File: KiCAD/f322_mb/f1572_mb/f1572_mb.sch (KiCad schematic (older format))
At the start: 24 parts, among them Q1 2N3904, SW1 power, SW2 ~rst, U1 PIC12F1572, U2 LM386

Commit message: debugging and adding melodies
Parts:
- removed C5: 1µF, symbol device:CP
- removed C6: 47n, symbol device:C
- removed C7: 220µF, symbol device:CP
- removed R4, R5, R6: 100R, symbol device:R
- removed RV1: 10K, symbol device:POT
- removed U2: LM386, symbol linear:LM386
- removed X?: 8Mhz, Oscillators:Oscillator_DIP-8, symbol Oscillators:CXO_DIP8
- added C1: 100µF, symbol device:CP
- added D1: 1N4001, symbol device:D
- added D2: RED, symbol device:LED
- added D3, D4: 1N4148, symbol device:D
- added D5, D6: GRN/RED, symbol device:LED_Dual_AAC
- added R2: 470R, symbol device:R
- added R3: 3K3, symbol device:R
- added R9: 220R, symbol device:R
- BT1: value 4,5v -> 6v
- C5: renamed from C4; value 220µF -> 100µF
- R8: value 10R -> 220R
- renumbered C1 to C2, C2 to C3, C3 to C4, R2 to R4, R3 to R5
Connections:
- net GND: now also R8.2, C1.2, R9.2; no longer R8.1
- net Vdd: now also D1.1 (K), R2.2; no longer SW1.2 (B)
- net at R4.2: now also U1.6 (RA1), R3.2; no longer U1.3 (RA4)
- net at U1.5 (RA2): now also D2.1 (K)
- net at U1.7 (RA0): now also Q1.2 (C)
- net at C4.1, R5.2: now also D3.2 (A), D4.1 (K); no longer R4.1
- net at LS1.1: now also C5.2
- net CLKIN renamed RA5
- net RA5: now also D5.1 (A1), D6.2 (A2)
- new net: D4.2 (A), R4.1
- new net: D2.2 (A), R2.1
- new net: D3.1 (K), R3.1
- new net: D5.3 (K), R8.1
- new net: D6.3 (K), R9.1
- new net RA4: D5.2 (A2), D6.1 (A1), U1.3 (RA4)
- new net Vbatt: C1.1, D1.2 (A), SW1.2 (B)
- no-connect marks 1 -> 0
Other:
- moved on the sheet: BT1, C4, LS1, R4, R5, SW1, SW2

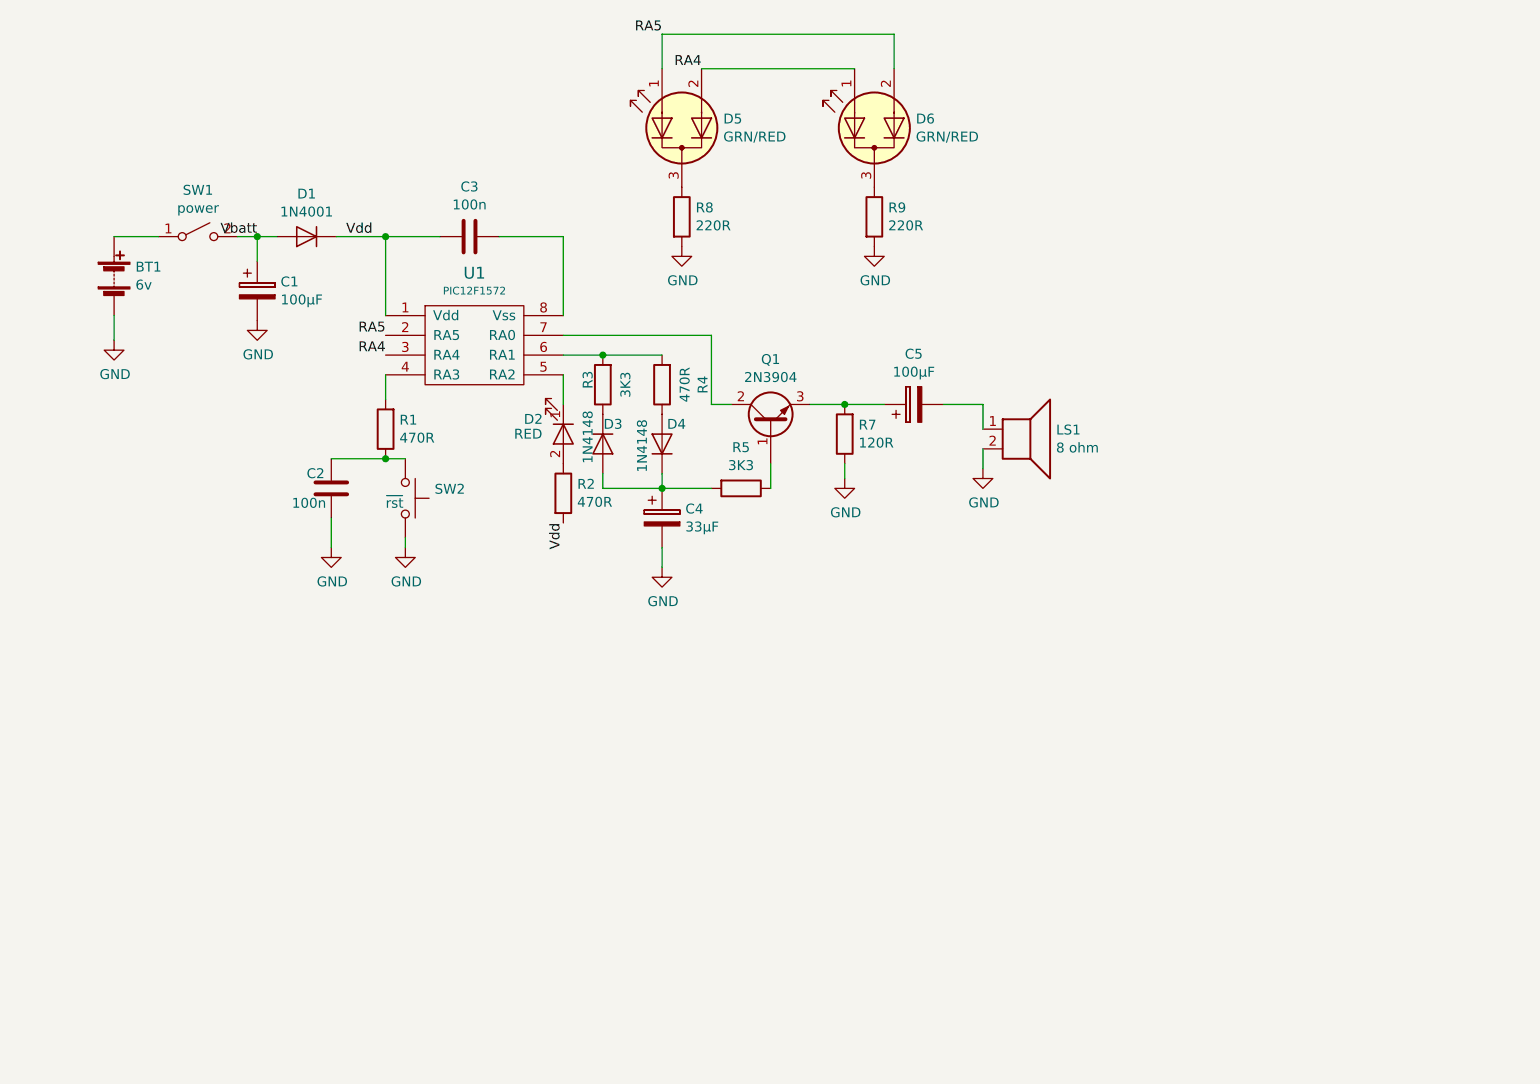
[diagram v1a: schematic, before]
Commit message: modification to cicircuit diagram. Switched PWM between LED and ENV
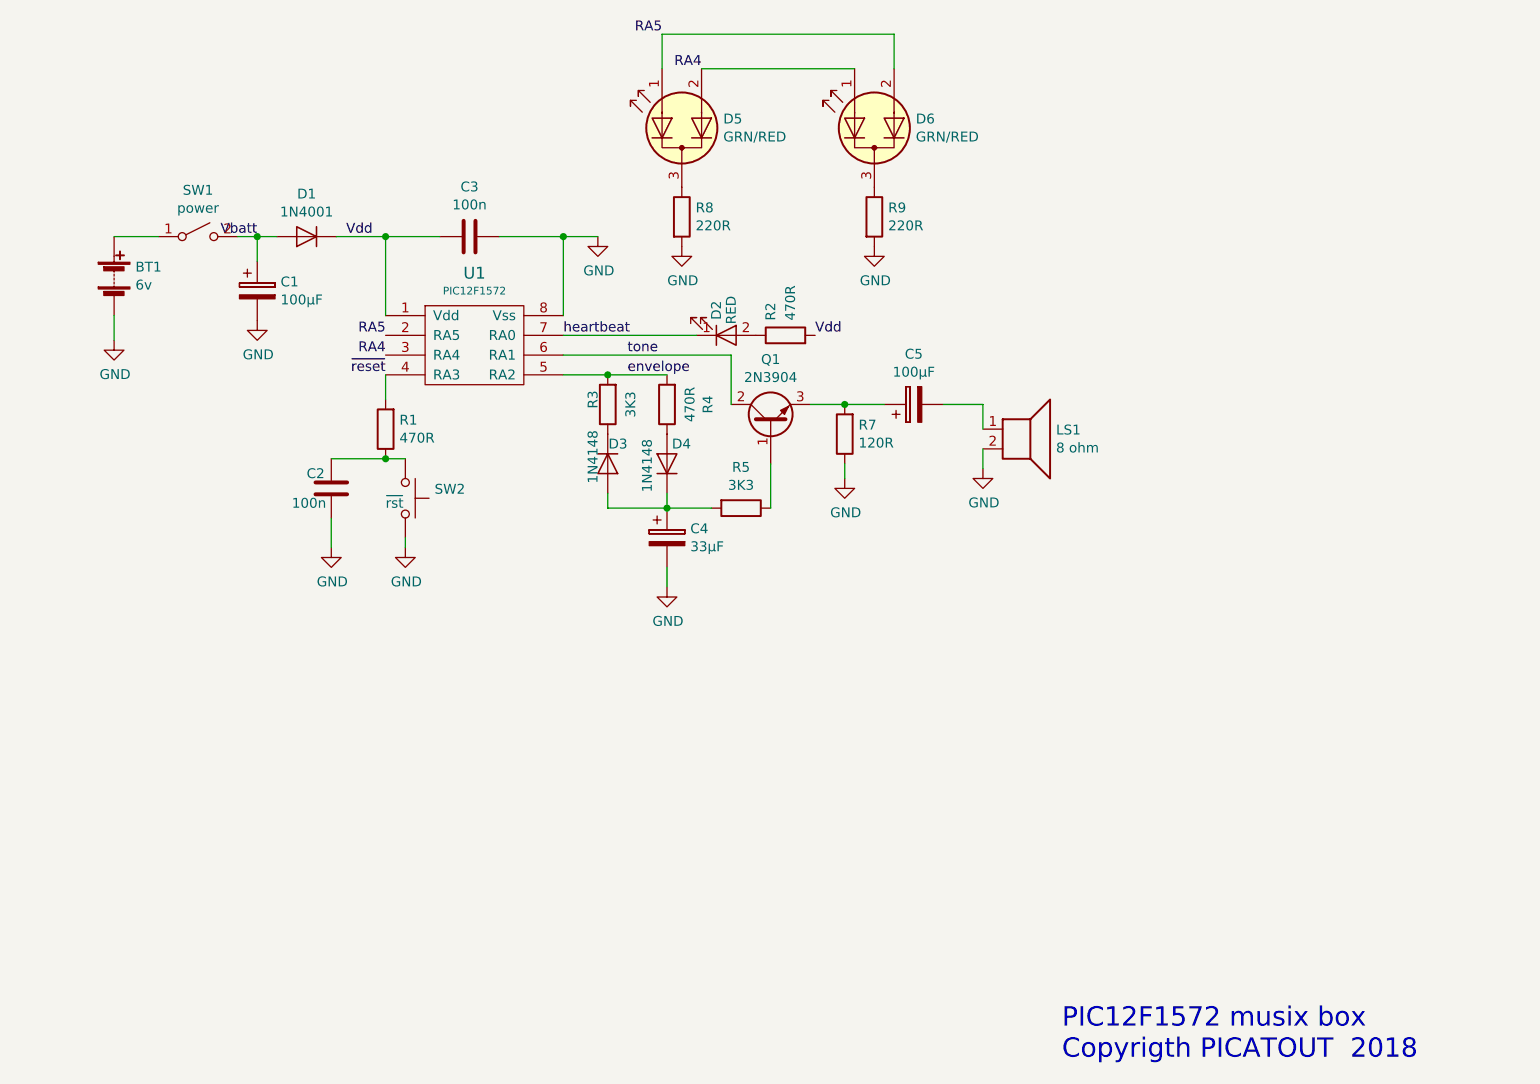
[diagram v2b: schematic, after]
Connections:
- net GND: now also C3.1, U1.8 (Vss)
- net ~reset: now reaches R1.2, U1.4 (RA3)
- net envelope: now reaches U1.5 (RA2)
- net envelope: now also R3.2, R4.2; no longer D2.1 (K)
- net heartbeat: now reaches U1.7 (RA0)
- net heartbeat: now also D2.1 (K); no longer Q1.2 (C)
- new net tone: Q1.2 (C), U1.6 (RA1)
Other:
- note added: "PIC12F1572 musix box\nCopyrigth PICATOUT 2018"
- moved on the sheet: C4, D2, D3, D4, R2, R3, R4, R5
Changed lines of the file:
@@
 	0    -1   -1   0
 $EndComp
-Wire Wire Line
-	5500 3275 5500 3625
-Wire Wire Line
-	5500 3625 5600 3625
 $Comp
 L device:R R7
@@
 L device:R R5
 U 1 1 5C07471B
-P 5650 4050
-F 0 "R5" V 5443 4050 50  0000 C CNN
-F 1 "3K3" V 5534 4050 50  0000 C CNN
-F 2 "" V 5580 4050 50  0001 C CNN
-F 3 "" H 5650 4050 50  0001 C CNN
-	1    5650 4050
+P 5650 4150
+F 0 "R5" V 5443 4150 50  0000 C CNN
+F 1 "3K3" V 5534 4150 50  0000 C CNN
+F 2 "" V 5580 4150 50  0001 C CNN
+F 3 "" H 5650 4150 50  0001 C CNN
+	1    5650 4150
 	0    1    1    0
 $EndComp
@@
 L device:CP C4
 U 1 1 5C07494D
-P 5250 4200
-F 0 "C4" H 5368 4246 50  0000 L CNN
-F 1 "33µF" H 5368 4155 50  0000 L CNN
-F 2 "" H 5288 4050 50  0001 C CNN
-F 3 "" H 5250 4200 50  0001 C CNN
-	1    5250 4200
+P 5275 4300
+F 0 "C4" H 5393 4346 50  0000 L CNN
+F 1 "33µF" H 5393 4255 50  0000 L CNN
+F 2 "" H 5313 4150 50  0001 C CNN
+F 3 "" H 5275 4300 50  0001 C CNN
+	1    5275 4300
 	1    0    0    -1
 $EndComp
@@
 L power:GND #PWR05
 U 1 1 5C0749C3
-P 5250 4450
-F 0 "#PWR05" H 5250 4200 50  0001 C CNN
-F 1 "GND" H 5255 4277 50  0000 C CNN
-F 2 "" H 5250 4450 50  0001 C CNN
-F 3 "" H 5250 4450 50  0001 C CNN
-	1    5250 4450
-	1    0    0    -1
-$EndComp
-Wire Wire Line
-	5250 4350 5250 4450
-Wire Wire Line
-	5250 4050 5500 4050
+P 5275 4550
+F 0 "#PWR05" H 5275 4300 50  0001 C CNN
+F 1 "GND" H 5280 4377 50  0000 C CNN
+F 2 "" H 5275 4550 50  0001 C CNN
+F 3 "" H 5275 4550 50  0001 C CNN
+	1    5275 4550
+	1    0    0    -1
+$EndComp
+Wire Wire Line
+	5275 4450 5275 4550
 $Comp
 L device:R R4
 U 1 1 5C074DC4
-P 5250 3525
-F 0 "R4" V 5043 3525 50  0000 C CNN
-F 1 "470R" V 5134 3525 50  0000 C CNN
-F 2 "" V 5180 3525 50  0001 C CNN
-F 3 "" H 5250 3525 50  0001 C CNN
-	1    5250 3525
+P 5275 3625
+F 0 "R4" V 5068 3625 50  0000 C CNN
+F 1 "470R" V 5159 3625 50  0000 C CNN
+F 2 "" V 5205 3625 50  0001 C CNN
+F 3 "" H 5275 3625 50  0001 C CNN
+	1    5275 3625
 	-1   0    0    1
 $EndComp
@@
 	6175 3625 6375 3625
 Connection ~ 6175 3625
-Wire Wire Line
-	4750 3275 5500 3275
-Wire Wire Line
-	5800 3925 5800 4050
-Connection ~ 5250 4050
-$Comp
-L device:LED D2
-U 1 1 5C099DC3
-P 4750 3775
-F 0 "D2" V 4675 3575 50  0000 L CNN
-F 1 "RED" V 4750 3525 50  0000 L CNN
-F 2 "" H 4750 3775 50  0001 C CNN
-F 3 "" H 4750 3775 50  0001 C CNN
-	1    4750 3775
-	0    1    1    0
-$EndComp
-Wire Wire Line
-	4750 3475 4750 3625
+Connection ~ 5275 4150
 $Comp
 L device:R R2
 U 1 1 5C09AC95
-P 4750 4075
-F 0 "R2" H 4820 4121 50  0000 L CNN
-F 1 "470R" H 4820 4030 50  0000 L CNN
-F 2 "" V 4680 4075 50  0001 C CNN
-F 3 "" H 4750 4075 50  0001 C CNN
-	1    4750 4075
-	1    0    0    -1
-$EndComp
-Text Label 4750 4225 3    50   ~ 0
+P 5875 3275
+F 0 "R2" H 5950 3350 50  0000 L CNN
+F 1 "470R" H 5950 3250 50  0000 L CNN
+F 2 "" V 5805 3275 50  0001 C CNN
+F 3 "" H 5875 3275 50  0001 C CNN
+	1    5875 3275
+	0    -1   -1   0
+$EndComp
+Text Label 6025 3275 0    50   ~ 0
 Vdd
 $Comp
 L device:D D4
 U 1 1 5C09B843
-P 5250 3825
-F 0 "D4" V 5350 3800 50  0000 R CNN
-F 1 "1N4148" H 5375 3925 50  0000 R CNN
-F 2 "" H 5250 3825 50  0001 C CNN
-F 3 "" H 5250 3825 50  0001 C CNN
-	1    5250 3825
-	0    -1   -1   0
-$EndComp
-Wire Wire Line
-	4750 3375 4950 3375
-Wire Wire Line
-	5250 3975 5250 4050
+P 5275 3925
+F 0 "D4" V 5375 3900 50  0000 R CNN
+F 1 "1N4148" H 5400 4025 50  0000 R CNN
+F 2 "" H 5275 3925 50  0001 C CNN
+F 3 "" H 5275 3925 50  0001 C CNN
+	1    5275 3925
+	0    -1   -1   0
+$EndComp
+Wire Wire Line
+	5275 4075 5275 4150
 $Comp
 L device:R R3
 U 1 1 5C0B54FF
-P 4950 3525
-F 0 "R3" V 5025 3500 50  0000 C CNN
-F 1 "3K3" V 4834 3525 50  0000 C CNN
-F 2 "" V 4880 3525 50  0001 C CNN
-F 3 "" H 4950 3525 50  0001 C CNN
-	1    4950 3525
-	-1   0    0    1
-$EndComp
-Connection ~ 4950 3375
-Wire Wire Line
-	4950 3375 5250 3375
+P 4975 3625
+F 0 "R3" V 5050 3600 50  0000 C CNN
+F 1 "3K3" V 4859 3625 50  0000 C CNN
+F 2 "" V 4905 3625 50  0001 C CNN
+F 3 "" H 4975 3625 50  0001 C CNN
+	1    4975 3625
+	-1   0    0    1
+$EndComp
+Wire Wire Line
+	4975 3475 5275 3475
 $Comp
 L device:D D3
 U 1 1 5C0B56CF
-P 4950 3825
-F 0 "D3" V 4850 3925 50  0000 R CNN
-F 1 "1N4148" H 5050 3750 50  0000 R CNN
-F 2 "" H 4950 3825 50  0001 C CNN
-F 3 "" H 4950 3825 50  0001 C CNN
-	1    4950 3825
+P 4975 3925
+F 0 "D3" V 4875 4025 50  0000 R CNN
+F 1 "1N4148" H 5075 3850 50  0000 R CNN
+F 2 "" H 4975 3925 50  0001 C CNN
+F 3 "" H 4975 3925 50  0001 C CNN
+	1    4975 3925
 	0    1    1    0
 $EndComp
 Wire Wire Line
-	4950 3975 4950 4050
-Wire Wire Line
-	4950 4050 5250 4050
+	4975 4075 4975 4150
+Wire Wire Line
+	4975 4150 5275 4150
 Text Label 5250 1750 2    50   ~ 0
 RA5
@@
 Wire Wire Line
 	3575 4200 3575 4350
+Text Notes 7275 6950 0    98   ~ 0
+PIC12F1572 musix box\nCopyrigth PICATOUT  2018
+$Comp
+L power:GND #PWR?
+U 1 1 5C0FEB96
+P 4925 2775
+F 0 "#PWR?" H 4925 2525 50  0001 C CNN
+F 1 "GND" H 4930 2602 50  0000 C CNN
+F 2 "" H 4925 2775 50  0001 C CNN
+F 3 "" H 4925 2775 50  0001 C CNN
+	1    4925 2775
+	1    0    0    -1
+$EndComp
+Wire Wire Line
+	4750 2775 4925 2775
+Connection ~ 4750 2775
+Wire Wire Line
+	4750 3475 4975 3475
+Connection ~ 4975 3475
+Wire Wire Line
+	5275 4150 5500 4150
+Wire Wire Line
+	5800 3925 5800 4150
+Text Label 5075 3375 0    50   ~ 0
+tone
+Text Label 5075 3475 0    50   ~ 0
+envelope
+Text Label 4750 3275 0    50   ~ 0
+heartbeat
+Text Label 3850 3475 2    50   ~ 0
+~reset
+$Comp
+L device:LED D2
+U 1 1 5C099DC3
+P 5575 3275
+F 0 "D2" V 5525 3100 50  0000 L CNN
+F 1 "RED" V 5600 3075 50  0000 L CNN
+F 2 "" H 5575 3275 50  0001 C CNN
+F 3 "" H 5575 3275 50  0001 C CNN
+	1    5575 3275
+	1    0    0    1
+$EndComp
+Wire Wire Line
+	4750 3375 5600 3375
+Wire Wire Line
+	5600 3375 5600 3625
+Wire Wire Line
+	4750 3275 5425 3275
 $EndSCHEMATC
